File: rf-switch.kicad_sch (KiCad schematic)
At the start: 1 part

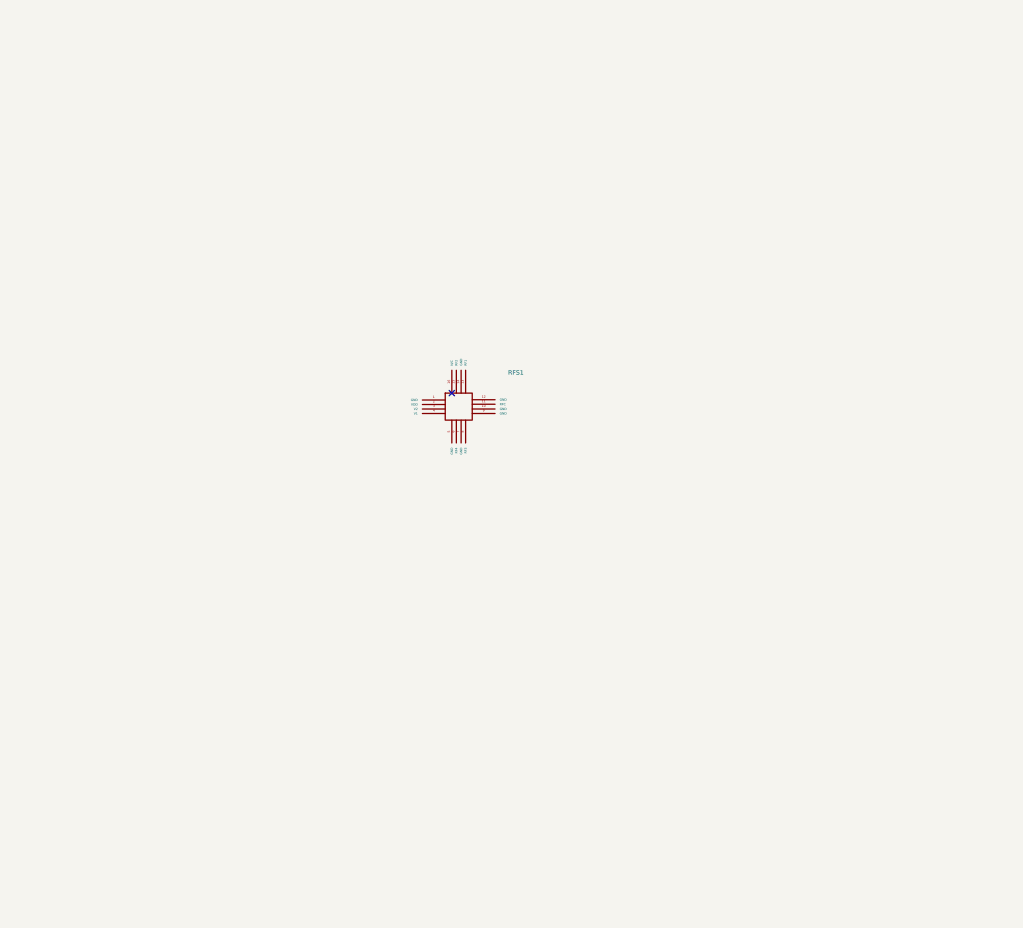
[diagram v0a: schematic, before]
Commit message: Schematic w/ footprints done
Need to do PCB layout
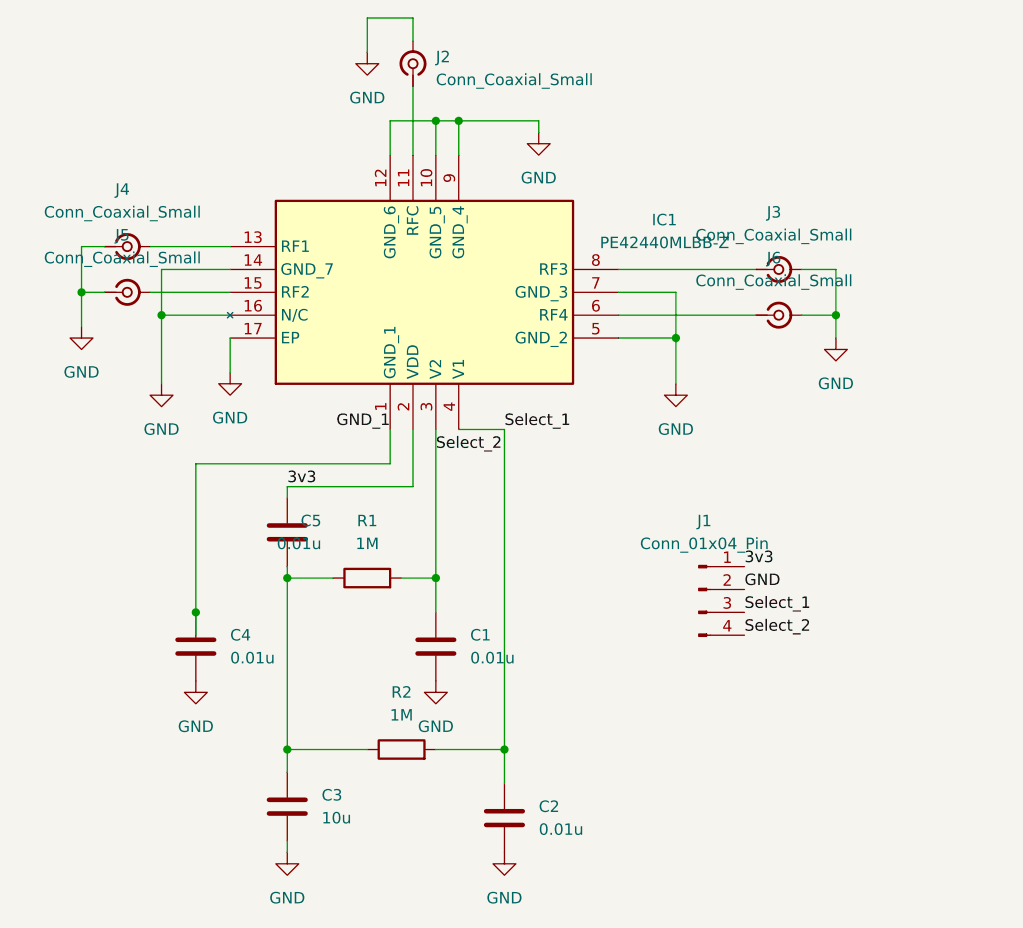
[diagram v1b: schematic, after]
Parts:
- removed RFS1: ~, PE42440_rf_switch:PE42440, symbol rf-switch:PE42440MLBB-Z
- added C1, C2, C4, C5: 0.01u, Capacitor_SMD:C_1206_3216Metric, symbol Device:C
- added C3: 10u, Capacitor_SMD:C_1206_3216Metric, symbol Device:C
- added IC1: PE42440MLBB-Z, PE42440_rf_switch:PE42440, symbol rf-switch:PE42440MLBB-Z
- added J1: Conn_01x04_Pin, Connector_PinHeader_2.54mm:PinHeader_1x04_P2.54mm_Vertical, symbol Connector:Conn_01x04_Pin
- added J2, J3, J4, J5, J6: Conn_Coaxial_Small, Connector_Coaxial:SMA_Amphenol_132289_EdgeMount, symbol Connector:Conn_Coaxial_Small
- added R1, R2: 1M, Resistor_SMD:R_1206_3216Metric, symbol Device:R
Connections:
- new net: IC1.15 (RF2), J5.2 (Ext)
- new net: IC1.6 (RF4), J6.1 (In)
- new net: C3.1, C5.2, R1.1, R2.1
- new net: IC1.13 (RF1), J4.2 (Ext)
- new net: IC1.8 (RF3), J3.1 (In)
- new net: IC1.11 (RFC), J2.1 (In)
- new net 3v3: C5.1, IC1.2 (VDD), J1.1 (Pin_1)
- new net GND: C1.2, C2.2, C3.2, C4.2, IC1.10 (GND_5), IC1.12 (GND_6), IC1.14 (GND_7), IC1.16 (N/C), IC1.17 (EP), IC1.5 (GND_2), IC1.7 (GND_3), IC1.9 (GND_4), J1.2 (Pin_2), J2.2 (Ext), J3.2 (Ext), J4.1 (In), J5.1 (In), J6.2 (Ext)
- new net GND_1: C4.1, IC1.1 (GND_1)
- new net Select_1: C2.1, IC1.4 (V1), J1.3 (Pin_3), R2.2
- new net Select_2: C1.1, IC1.3 (V2), J1.4 (Pin_4), R1.2

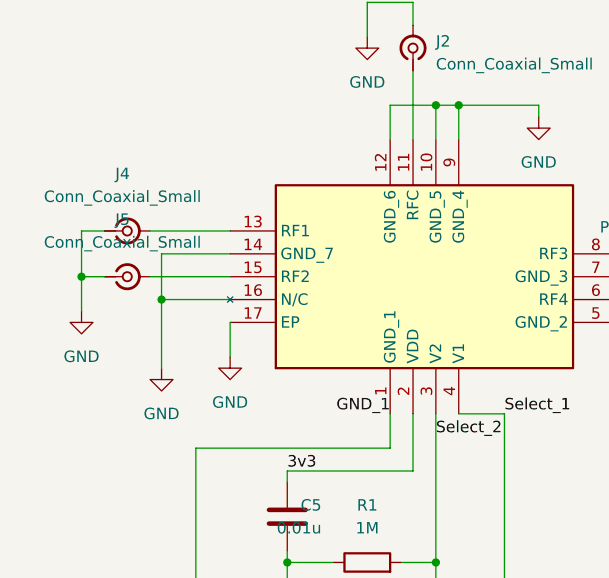
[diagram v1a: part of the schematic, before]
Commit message: Semi-completed PCB Schematic
Done wiring some of the components. Still need to finish this.
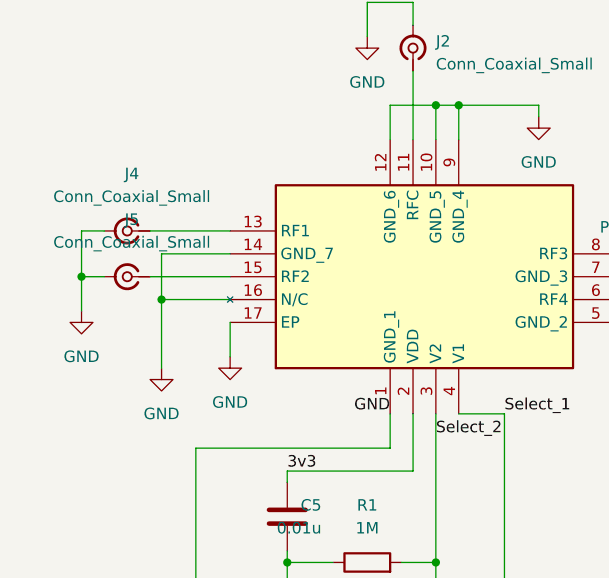
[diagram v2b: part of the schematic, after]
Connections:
- net GND_1 is gone; now on net GND: C4.1, IC1.1 (GND_1)
- net GND: now also J4.2 (Ext), J5.2 (Ext); no longer J4.1 (In), J5.1 (In)
- net at IC1.15 (RF2): now also J5.1 (In); no longer J5.2 (Ext)
- net at IC1.13 (RF1): now also J4.1 (In); no longer J4.2 (Ext)
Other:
- moved on the sheet: J4, J5
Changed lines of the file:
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@@
 		)
 	)
-	(label "GND_1"
+	(label "GND"
 		(at 133.35 91.44 180)
 		(effects
@@
 	(symbol
 		(lib_id "Connector:Conn_Coaxial_Small")
-		(at 104.14 76.2 0)
+		(at 104.14 76.2 180)
 		(unit 1)
 		(exclude_from_sim no)
@@
 		(fields_autoplaced yes)
 		(property "Reference" "J5"
-			(at 103.6204 69.85 0)
+			(at 104.6595 69.85 0)
 			(effects
 				(font
@@
 		)
 		(property "Value" "Conn_Coaxial_Small"
-			(at 103.6204 72.39 0)
+			(at 104.6595 72.39 0)
 			(effects
 				(font
@@
 	(symbol
 		(lib_id "Connector:Conn_Coaxial_Small")
-		(at 104.14 71.12 0)
+		(at 104.14 71.12 180)
 		(unit 1)
 		(exclude_from_sim no)
@@
 		(fields_autoplaced yes)
 		(property "Reference" "J4"
-			(at 103.6204 64.77 0)
+			(at 104.6595 64.77 0)
 			(effects
 				(font
@@
 		)
 		(property "Value" "Conn_Coaxial_Small"
-			(at 103.6204 67.31 0)
-			(effects
-				(font
+			(at 104.6595 67.31 0)
+			(effects
+				(font

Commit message: PCB layout is done
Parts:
- removed C5: 0.01u, Capacitor_SMD:C_1206_3216Metric, symbol Device:C
- C2: value 0.01u -> 10u
- C3: value 10u -> 0.01u
- R1, R2: value 1M -> 10k
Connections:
- net 3v3: now also C2.2; no longer IC1.2 (VDD)
- net GND: now also R1.2, R2.2; no longer C1.2, C2.2, C4.1, IC1.16 (N/C)
- net Select_1: now also C4.1, R2.1; no longer C2.1, R2.2
- net Select_2: now also C3.1, R1.1; no longer C1.1, R1.2
- new net: C1.1, IC1.2 (VDD)
- new net: C1.2, C2.1
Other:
- moved on the sheet: J1
